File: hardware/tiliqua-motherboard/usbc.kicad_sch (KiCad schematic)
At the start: 9 parts, among them J7 USB_C_Receptacle_USB2.0_14P, U8 TUSB322I, U9 AP2161W

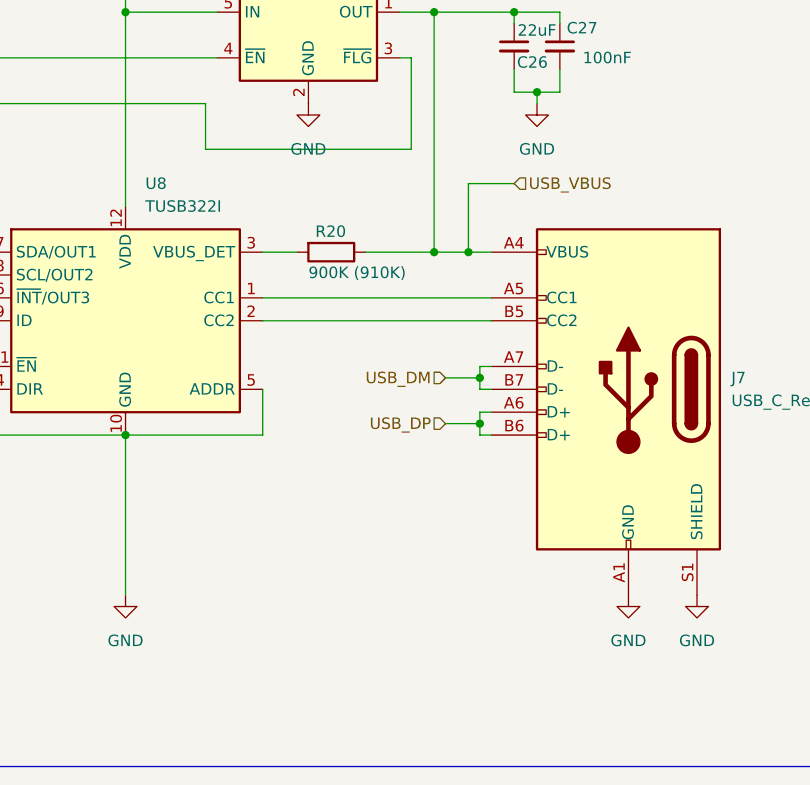
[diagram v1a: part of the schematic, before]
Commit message: * USB1/USB2 ESD protection
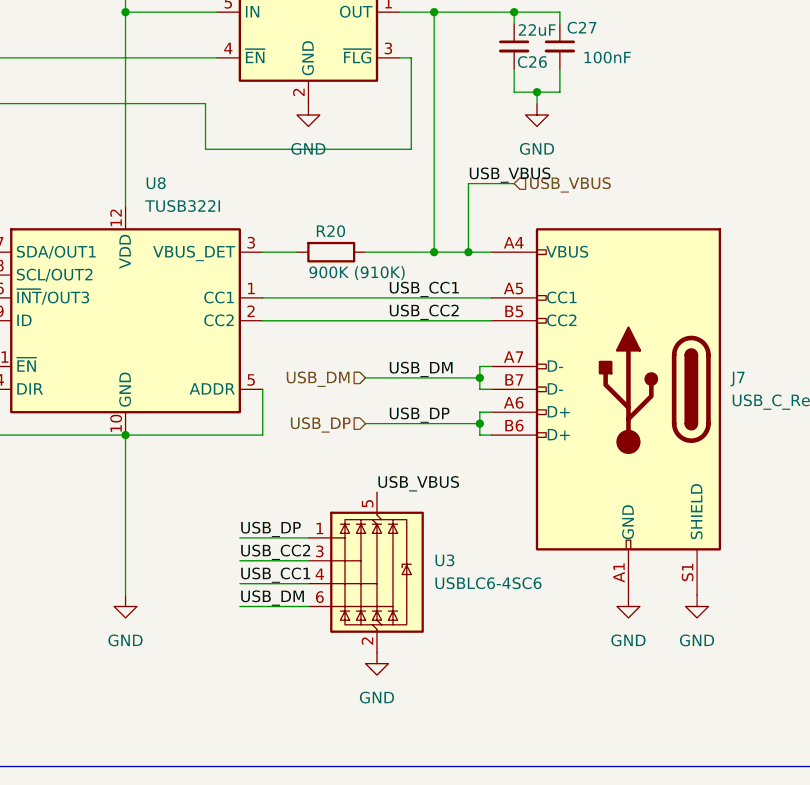
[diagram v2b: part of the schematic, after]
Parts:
- added U3: USBLC6-4SC6, Package_TO_SOT_SMD:SOT-23-6, symbol Power_Protection:USBLC6-4SC6
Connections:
- net GND: now also U3.2 (GND)
- net USB_DM: now also U3.6 (I/O4)
- net USB_DP: now also U3.1 (I/O1)
- net USB_VBUS: now also U3.5 (VBUS)
- net USB_CC1: now reaches J7.A5 (CC1), U8.1 (CC1)
- net USB_CC1: now also U3.4 (I/O3)
- net USB_CC2: now reaches J7.B5 (CC2), U8.2 (CC2)
- net USB_CC2: now also U3.3 (I/O2)

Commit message: * BOM: update some LCSC fields
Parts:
- U3: LCSC (none) -> C111212
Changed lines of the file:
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@@
+			)
+		)
+		(property "LCSC" "C111212"
+			(at 175.26 115.57 0)
+			(effects
+				(font
+					(size 1.27 1.27)
+				)
+				(hide yes)
 			)
 		)
